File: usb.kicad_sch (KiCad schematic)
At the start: 147 parts, among them J1 USB4105-GF-A, J4 WE_632723300011_alt_symbol, U3 TUSB1046-DCI, U4 CY7C65632-28LTXCT

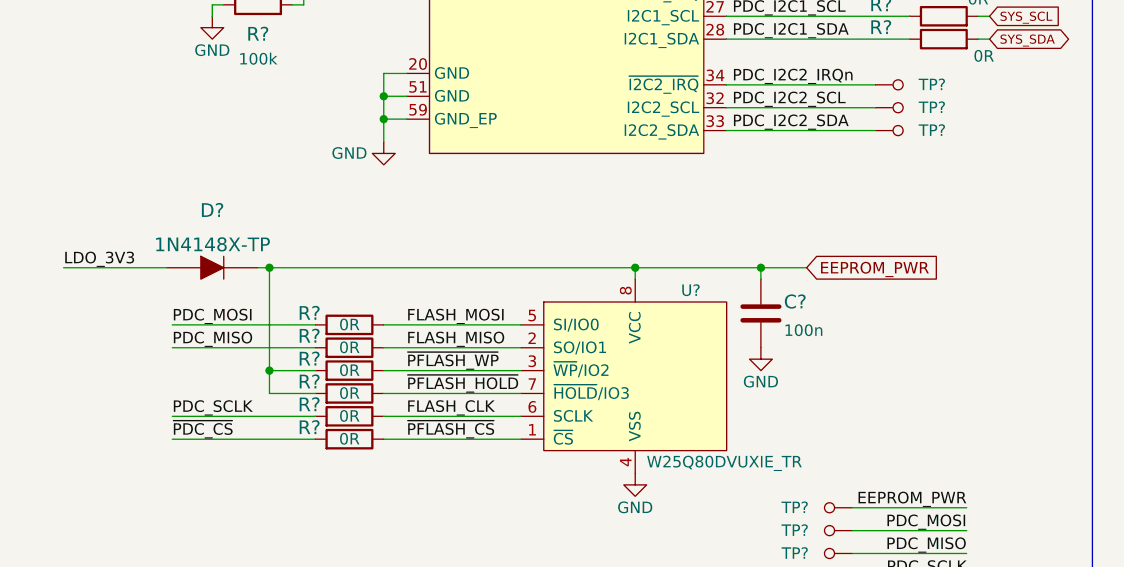
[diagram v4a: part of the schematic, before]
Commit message: Finished designing toggle button power-up, sequencing and reset circuitry with auto startup option
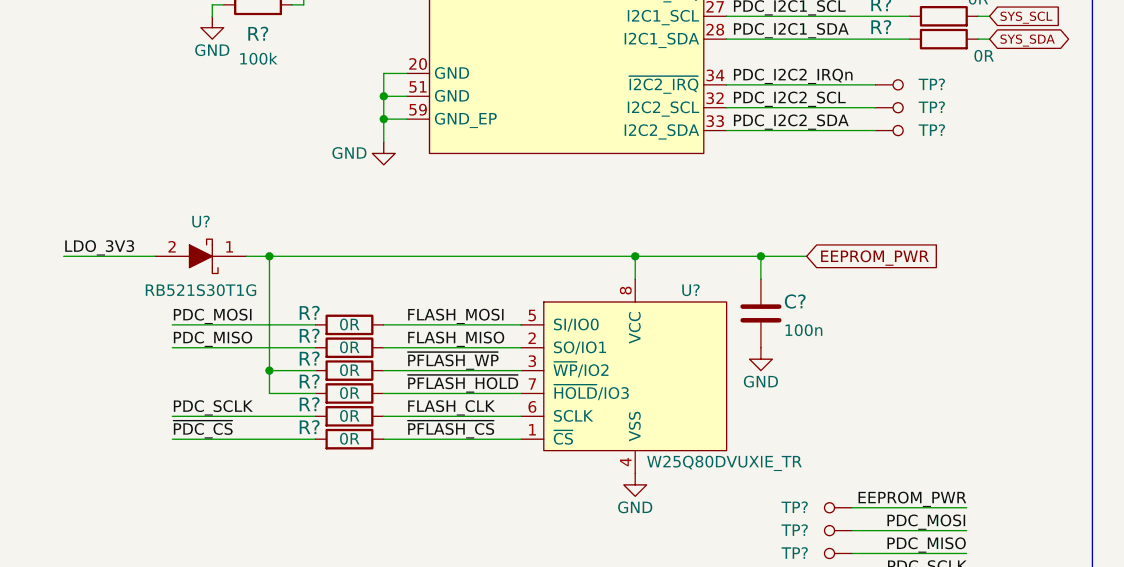
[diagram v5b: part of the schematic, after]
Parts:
- removed D?: 1N4148X-TP, antmicro-footprints:SOD-523, symbol antmicroDiodesRectifiersSingle:1N4148X-TP
- added U?: RB521S30T1G, antmicro-footprints:SOD-523, symbol antmicroDiodesRectifiersSingle:RB521S30T1G
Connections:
- net EEPROM_PWR: now also U?.1
- net LDO_3V3: now also U?.2
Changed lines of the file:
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@@
   (junction (at 252.73 222.25) (diameter 0) (color 0 0 0 0)
   )
-  (junction (at 81.28 237.49) (diameter 0) (color 0 0 0 0)
+  (junction (at 81.28 236.22) (diameter 0) (color 0 0 0 0)
   )
   (junction (at 312.42 59.69) (diameter 0) (color 0 0 0 0)
@@
   (junction (at 35.56 102.87) (diameter 0) (color 0 0 0 0)
   )
-  (junction (at 95.25 237.49) (diameter 0) (color 0 0 0 0)
+  (junction (at 95.25 236.22) (diameter 0) (color 0 0 0 0)
   )
   (junction (at 82.55 64.77) (diameter 0) (color 0 0 0 0)
@@
   (junction (at 269.24 146.05) (diameter 0) (color 0 0 0 0)
   )
-  (junction (at 40.64 237.49) (diameter 0) (color 0 0 0 0)
+  (junction (at 40.64 236.22) (diameter 0) (color 0 0 0 0)
   )
   (junction (at 127 196.85) (diameter 0) (color 0 0 0 0)
@@
     (stroke (width 0) (type default) (color 0 0 0 0))
   )
-  (wire (pts (xy 39.37 237.49) (xy 40.64 237.49))
+  (wire (pts (xy 38.1 236.22) (xy 40.64 236.22))
     (stroke (width 0) (type default) (color 0 0 0 0))
   )
@@
     (stroke (width 0) (type default) (color 0 0 0 0))
   )
-  (wire (pts (xy 17.78 237.49) (xy 29.21 237.49))
+  (wire (pts (xy 17.78 236.22) (xy 27.94 236.22))
     (stroke (width 0) (type default) (color 0 0 0 0))
   )
@@
     (stroke (width 0) (type default) (color 0 0 0 0))
   )
-  (wire (pts (xy 40.64 237.49) (xy 81.28 237.49))
+  (wire (pts (xy 40.64 236.22) (xy 81.28 236.22))
     (stroke (width 0) (type default) (color 0 0 0 0))
   )
@@
     (stroke (width 0) (type default) (color 0 0 0 0))
   )
-  (wire (pts (xy 95.25 237.49) (xy 100.33 237.49))
+  (wire (pts (xy 95.25 236.22) (xy 100.33 236.22))
     (stroke (width 0) (type default) (color 0 0 0 0))
   )
@@
     (stroke (width 0) (type default) (color 0 0 0 0))
   )
+  (wire (pts (xy 95.25 236.22) (xy 95.25 238.76))
+    (stroke (width 0) (type default) (color 0 0 0 0))
+  )
   (wire (pts (xy 228.6 85.09) (xy 262.89 85.09))
     (stroke (width 0) (type default) (color 0 0 0 0))
@@
     (stroke (width 0) (type default) (color 0 0 0 0))
   )
-  (wire (pts (xy 81.28 237.49) (xy 81.28 238.76))
+  (wire (pts (xy 81.28 236.22) (xy 81.28 238.76))
     (stroke (width 0) (type default) (color 0 0 0 0))
   )
@@
     (stroke (width 0) (type default) (color 0 0 0 0))
   )
-  (wire (pts (xy 95.25 237.49) (xy 95.25 238.76))
-    (stroke (width 0) (type default) (color 0 0 0 0))
-  )
   (wire (pts (xy 265.43 140.97) (xy 269.24 140.97))
     (stroke (width 0) (type default) (color 0 0 0 0))
@@
     (stroke (width 0) (type default) (color 0 0 0 0))
   )
-  (wire (pts (xy 40.64 237.49) (xy 40.64 248.92))
+  (wire (pts (xy 40.64 236.22) (xy 40.64 248.92))
     (stroke (width 0) (type default) (color 0 0 0 0))
   )
@@
     (stroke (width 0) (type default) (color 0 0 0 0))
   )
-  (wire (pts (xy 81.28 237.49) (xy 95.25 237.49))
+  (wire (pts (xy 81.28 236.22) (xy 95.25 236.22))
     (stroke (width 0) (type default) (color 0 0 0 0))
   )
@@
     (effects (font (size 1.1 1.1)) (justify right bottom))
   )
-  (label "LDO_3V3" (at 17.78 237.49 0)
+  (label "LDO_3V3" (at 17.78 236.22 0)
     (effects (font (size 1.27 1.27)) (justify left bottom))
   )
@@
     )
   )
-  (global_label "EEPROM_PWR" (shape input) (at 100.33 237.49 0) (fields_autoplaced)
+  (global_label "EEPROM_PWR" (shape input) (at 100.33 236.22 0) (fields_autoplaced)
     (effects (font (size 1.27 1.27)) (justify left))
-    (property "Intersheet References" "${INTERSHEET_REFS}" (id 0) (at 115.3221 237.4106 0)
+    (property "Intersheet References" "${INTERSHEET_REFS}" (id 0) (at 115.3221 236.1406 0)
       (effects (font (size 1.27 1.27)) (justify left) hide)
     )
@@
     (pin "1")
   )
-  (symbol (lib_id "antmicroDiodesRectifiersSingle:1N4148X-TP") (at 34.29 237.49 0) (unit 1)
-    (in_bom yes) (on_board yes) (fields_autoplaced)
-    (property "Reference" "D?" (id 0) (at 34.29 231.14 0)
-      (effects (font (size 1.524 1.524)))
-    )
-    (property "Value" "1N4148X-TP" (id 1) (at 34.29 234.95 0)
-      (effects (font (size 1.524 1.524)))
-    )
-    (property "Footprint" "antmicro-footprints:SOD-523" (id 2) (at 39.37 232.41 0)
-      (effects (font (size 1.524 1.524)) (justify left) hide)
-    )
-    (property "Datasheet" "https://www.mccsemi.com/pdf/Products/1N4148X(SOD-523).PDF" (id 3) (at 39.37 229.87 0)
-      (effects (font (size 1.524 1.524)) (justify left) hide)
-    )
-    (property "MPN" "1N4148X-TP" (id 4) (at 39.37 224.79 0)
-      (effects (font (size 1.524 1.524)) (justify left) hide)
-    )
-    (property "Manufacturer" "Micro Commercial Co" (id 5) (at 39.37 209.55 0)
-      (effects (font (size 1.524 1.524)) (justify left) hide)
-    )
-    (pin "A")
-    (pin "K")
-  )
   (symbol (lib_name "TPD4E05U06QDQARQ1_3") (lib_id "antmicroTVSDiodes:TPD4E05U06QDQARQ1") (at 336.55 232.41 270) (unit 1)
     (in_bom yes) (on_board yes)
@@
     (pin "1")
     (pin "2")
+  )
+  (symbol (lib_id "antmicroDiodesRectifiersSingle:RB521S30T1G") (at 33.02 236.22 0) (unit 1)
+    (in_bom yes) (on_board yes)
+    (property "Reference" "U?" (id 0) (at 33.02 232.41 0))
+    (property "Value" "RB521S30T1G" (id 1) (at 33.02 240.03 0))
+    (property "Footprint" "antmicro-footprints:SOD-523" (id 2) (at 35.56 243.84 0)
+      (effects (font (size 1.27 1.27)) hide)
+    )
+    (property "Datasheet" "https://www.mouser.pl/datasheet/2/308/RB521S30T1_D-1522497.pdf" (id 3) (at 35.56 243.84 0)
+      (effects (font (size 1.27 1.27)) hide)
+    )
+    (property "MPN" "RB521S30T1G" (id 4) (at 33.02 243.84 0)
+      (effects (font (size 1.27 1.27)) hide)
+    )
+    (property "Manufacturer" "onsemi" (id 5) (at 33.02 243.84 0)
+      (effects (font (size 1.27 1.27)) hide)
+    )
+    (pin "1")
+    (pin "2")

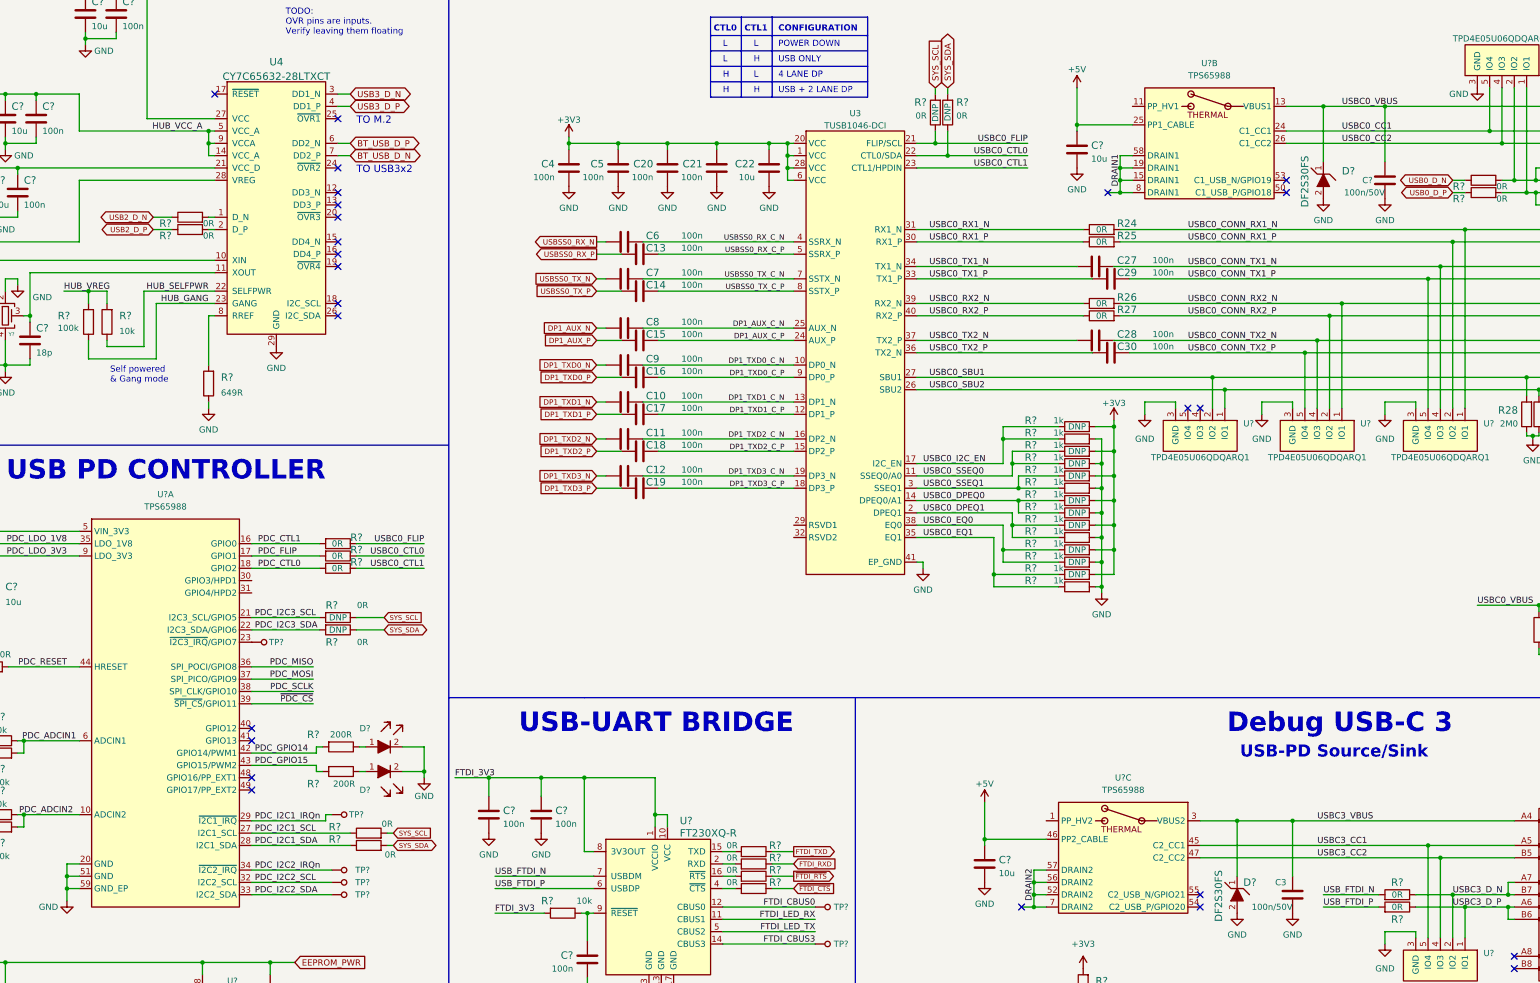
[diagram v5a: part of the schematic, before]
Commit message: Add inter-sheets references
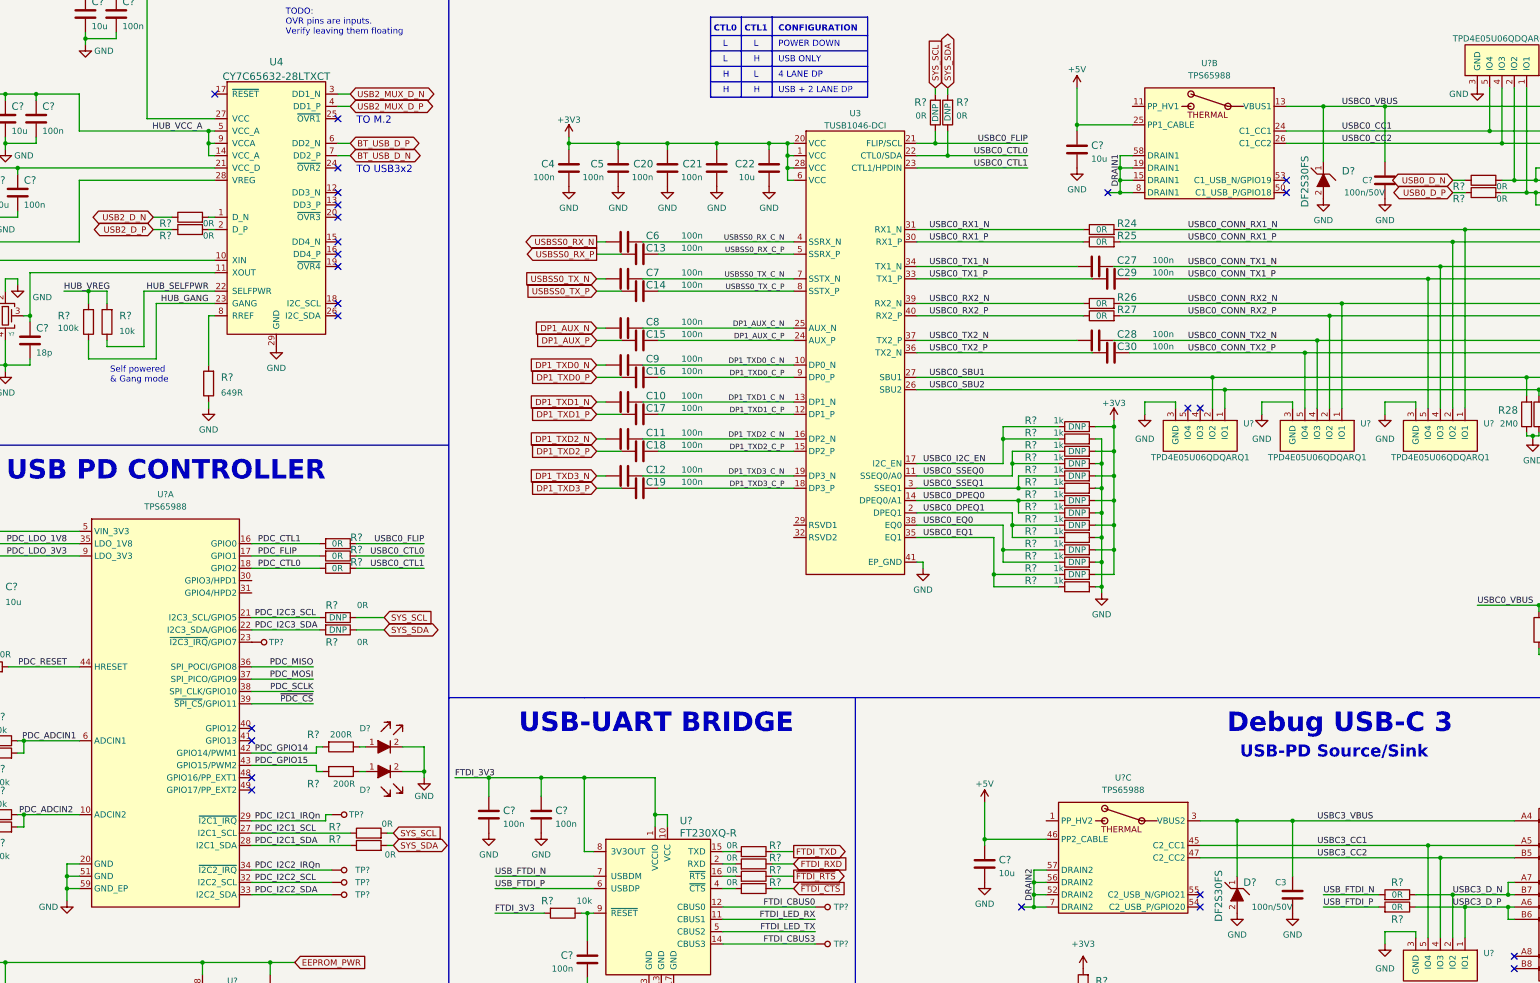
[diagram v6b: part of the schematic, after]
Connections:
- net USB3_D_N renamed USB2_MUX_D_N
- net USB3_D_P renamed USB2_MUX_D_P

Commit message: Improve usb subsheet readability
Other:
- moved on the sheet: C3, C?, D?, R?, TP?, U?, U?B

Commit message: Added soft power button and annotated schematic
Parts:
- gave numbers to parts that had none: 111
- renumbered C4 to C414, C5 to C416, C6 to C417, C7 to C418, C8 to C419, C9 to C420, C10 to C421, C11 to C422, C12 to C423, C13 to C424, C14 to C425, C15 to C426, C16 to C427, C17 to C428, C18 to C429, C19 to C430, C20 to C432, C21 to C433, C22 to C435, C27 to C439, C28 to C440, C29 to C441, C30 to C442, C3 to C444, J1 to J401, J4 to J402, R24 to R451, R25 to R452, R26 to R453, R27 to R454, R28 to R459, R29 to R460, U4 to U404, U3 to U407
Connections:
- net ~{FTDI_RTS} renamed PWR_SOFT
